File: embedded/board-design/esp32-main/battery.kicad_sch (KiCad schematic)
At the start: 1 part, among them U4 LTC4055

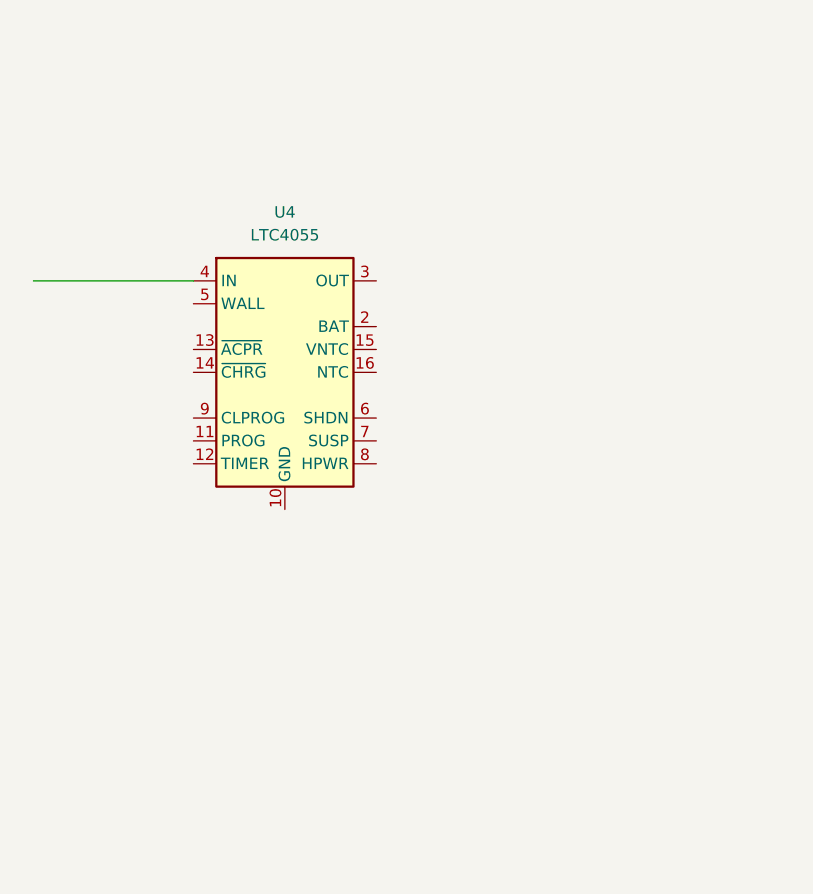
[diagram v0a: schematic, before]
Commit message: [bike-embedded-app]
Finished first schematic draft.

Signed-off-by: Nicolae-Andrei Vasile <vasilenicolaeandrei@gmail.com>
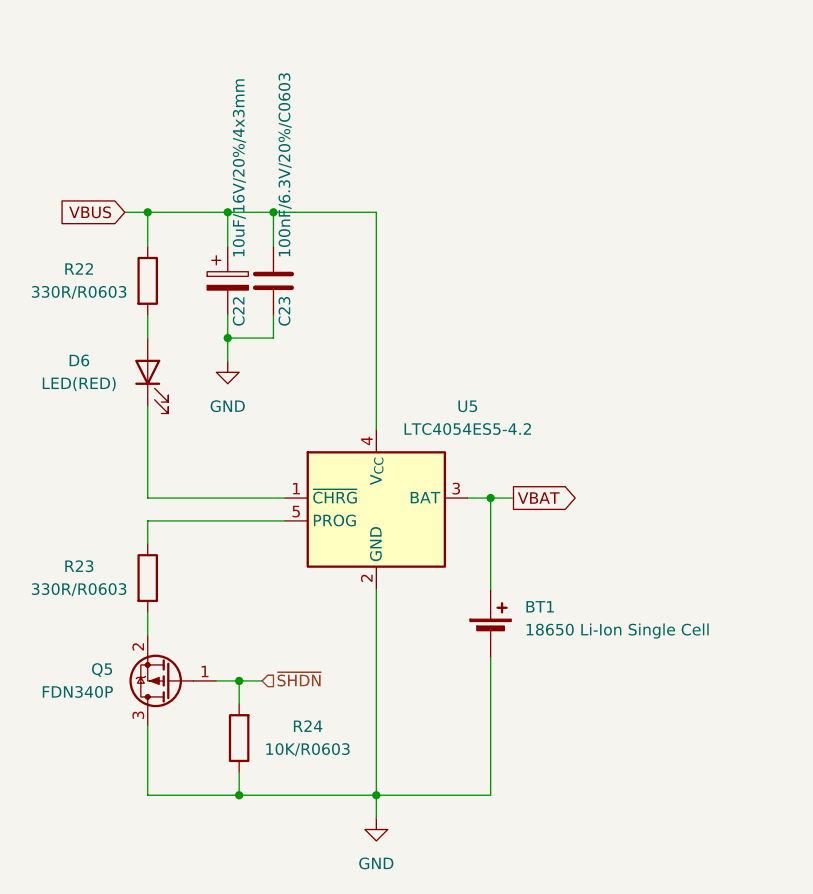
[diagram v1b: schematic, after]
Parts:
- removed U4: LTC4055, Package_DFN_QFN:QFN-16-1EP_4x4mm_P0.65mm_EP2.15x2.15mm, symbol Battery_Management:LTC4055
- added BT1: 18650 Li-Ion Single Cell, Battery:BatteryHolder_Keystone_1042_1x18650, symbol Device:Battery_Cell
- added C22: 10uF/16V/20%/4x3mm, Capacitor_SMD:CP_Elec_4x3, symbol Device:C_Polarized
- added C23: 100nF/6.3V/20%/C0603, Capacitor_SMD:C_0603_1608Metric_Pad1.08x0.95mm_HandSolder, symbol Device:C
- added D6: LED(RED), LED_SMD:LED_0603_1608Metric_Pad1.05x0.95mm_HandSolder, symbol Device:LED
- added Q5: FDN340P, Package_TO_SOT_SMD:SOT-23, symbol Transistor_FET:FDN340P
- added R22, R23: 330R/R0603, Resistor_SMD:R_0603_1608Metric_Pad0.98x0.95mm_HandSolder, symbol Device:R
- added R24: 10K/R0603, Resistor_SMD:R_0603_1608Metric_Pad0.98x0.95mm_HandSolder, symbol Device:R
- added U5: LTC4054ES5-4.2, Package_TO_SOT_SMD:TSOT-23-5, symbol Battery_Management:LTC4054ES5-4.2
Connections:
- new net: D6.2 (A), R22.2
- new net: Q5.2 (S), R23.2
- new net: D6.1 (K), U5.1 (~{CHRG})
- new net: R23.1, U5.5 (PROG)
- new net GND: BT1.2 (-), C22.2, C23.2, Q5.3 (D), R24.1, U5.2 (GND)
- new net VBAT: BT1.1 (+), U5.3 (BAT)
- new net VBUS: C22.1, C23.1, R22.1, U5.4 (V_{CC})
- new net ~{SHDN}: Q5.1 (G), R24.2

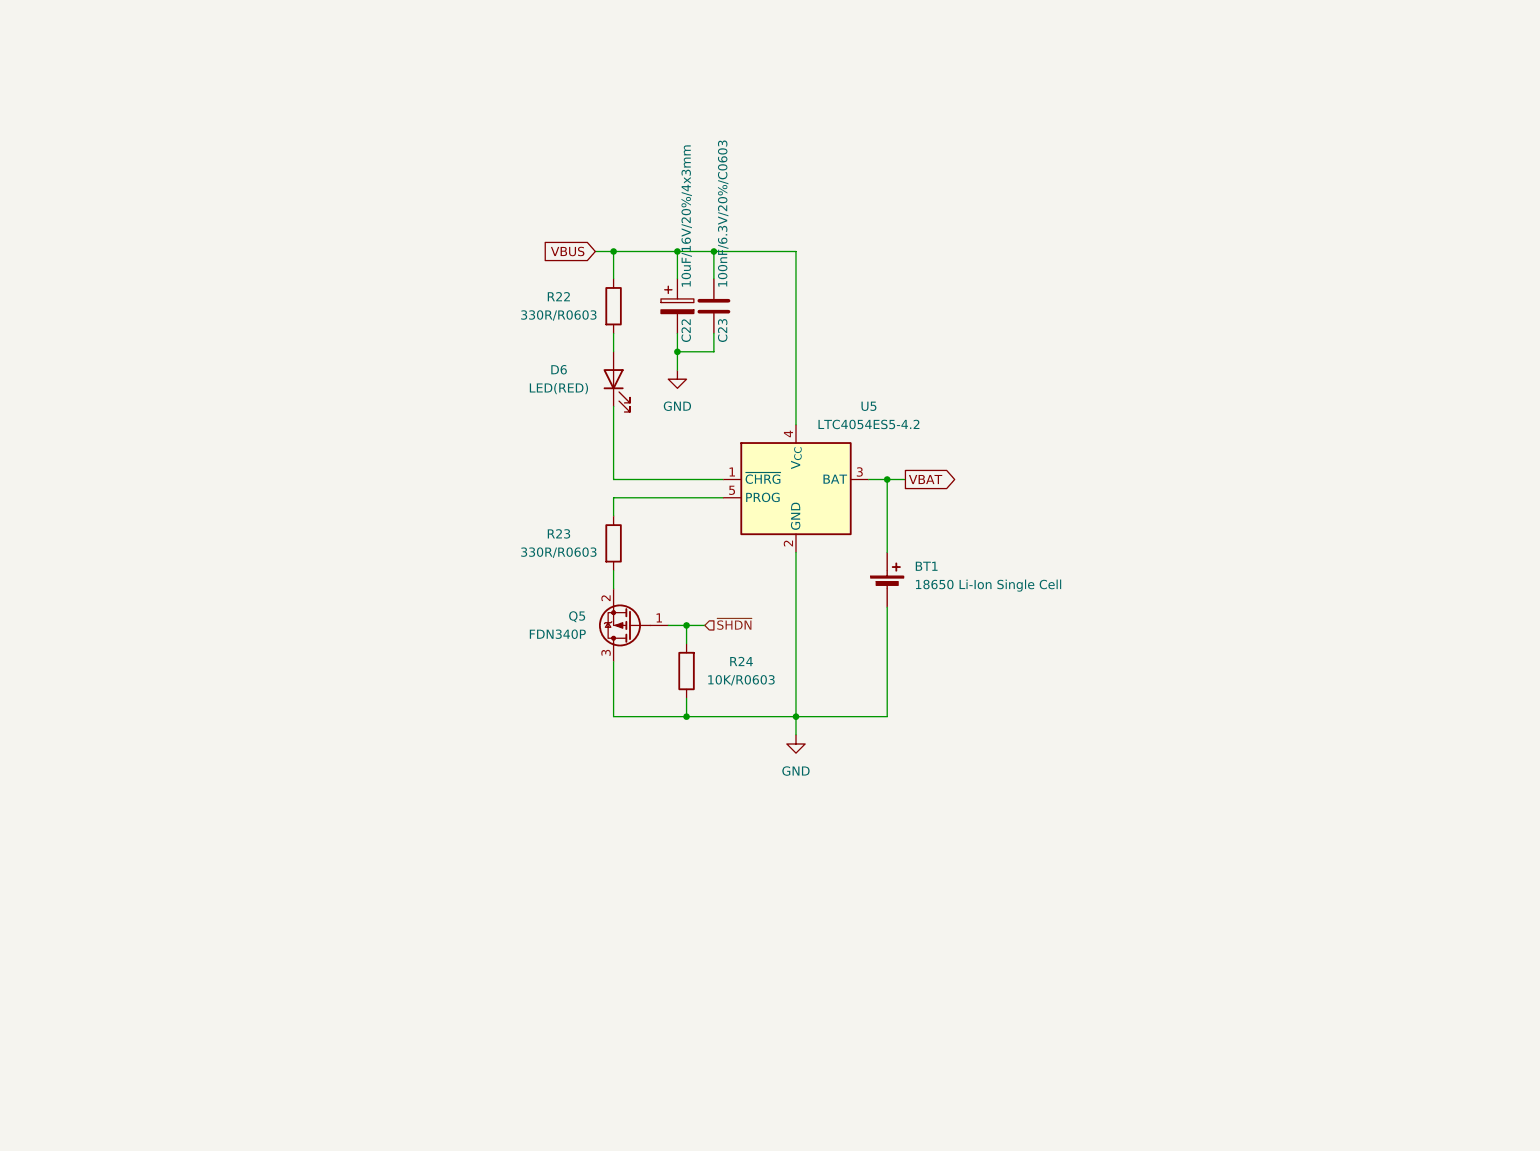
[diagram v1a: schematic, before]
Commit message: [bike-embedded-app]
First draft of the part placement on PCB. No routes drawn yet. Added
entry for possible alternator.

Signed-off-by: Nicolae-Andrei Vasile <vasilenicolaeandrei@gmail.com>
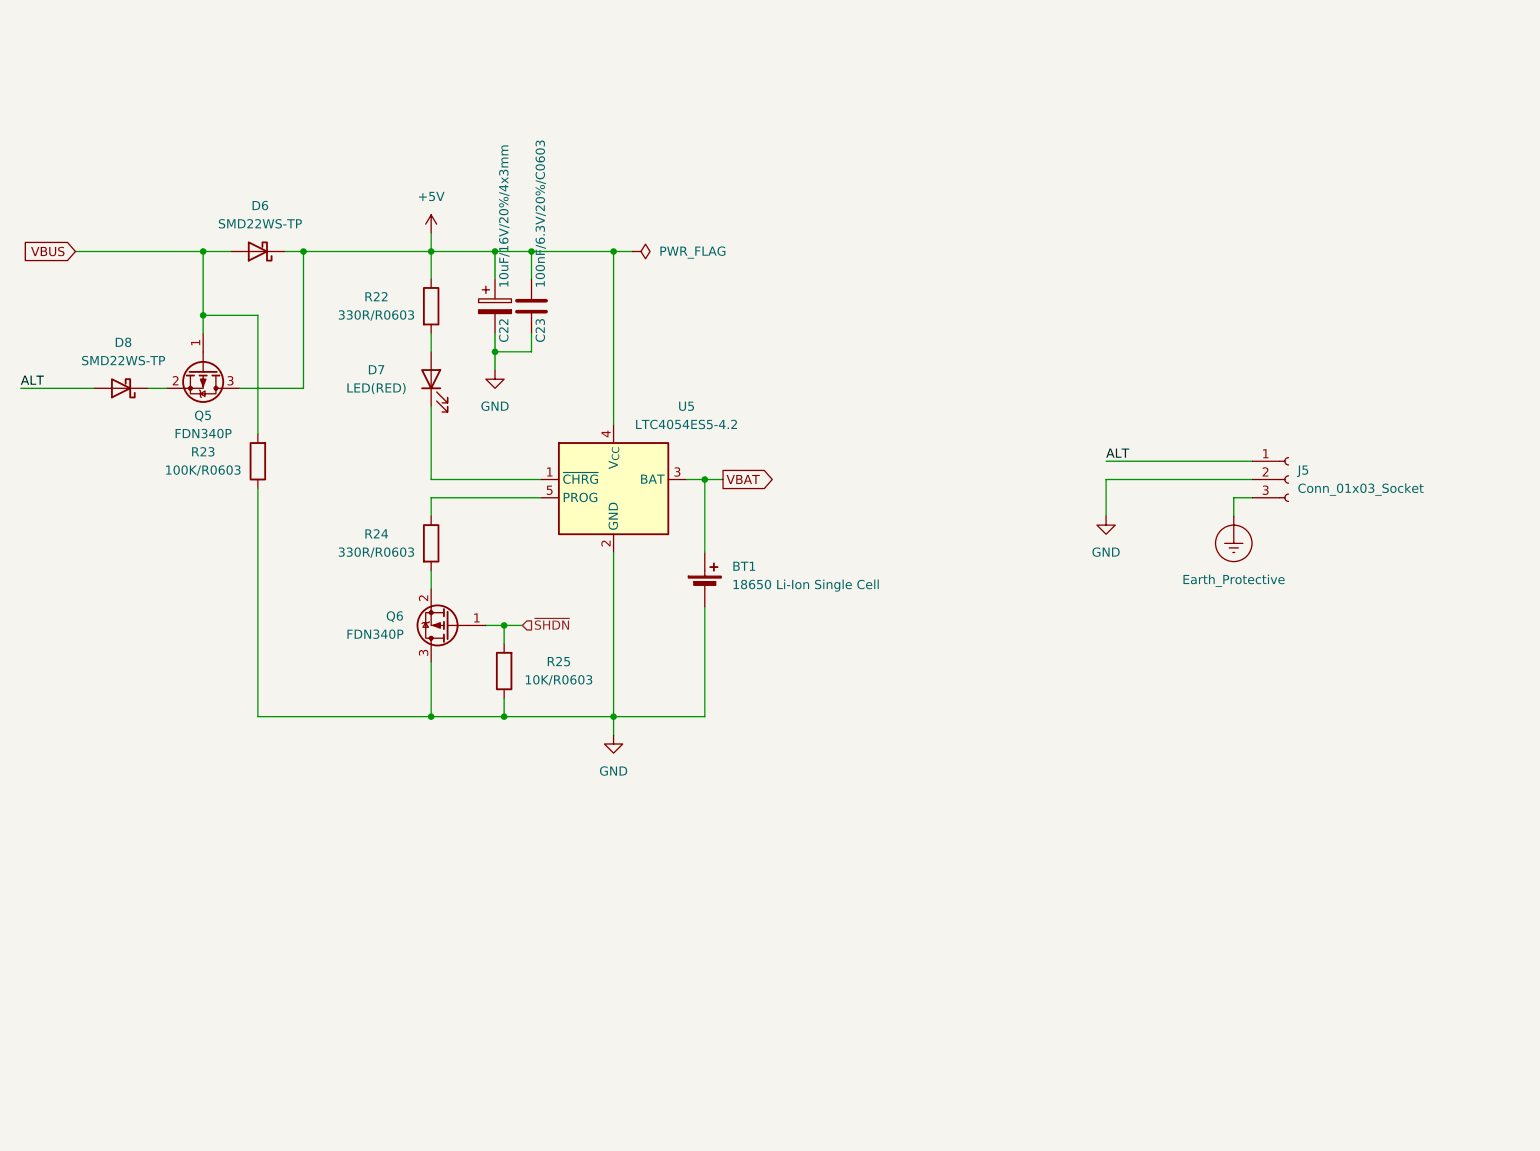
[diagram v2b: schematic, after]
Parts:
- added D6, D8: SMD22WS-TP, Diode_SMD:D_SOD-323_HandSoldering, symbol Device:D_Schottky
- added J5: Conn_01x03_Socket, Connector_Phoenix_MC:PhoenixContact_MC_1,5_3-G-3.81_1x03_P3.81mm_Horizontal, symbol Connector:Conn_01x03_Socket
- added Q5: FDN340P, Package_TO_SOT_SMD:SOT-23, symbol Transistor_FET:FDN340P
- added R23: 100K/R0603, Resistor_SMD:R_0603_1608Metric_Pad0.98x0.95mm_HandSolder, symbol Device:R
- renumbered D6 to D7, Q5 to Q6, R23 to R24, R24 to R25
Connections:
- net GND: now also J5.2 (Pin_2), R23.1
- net VBUS: now also D6.2 (A), Q5.1 (G), R23.2; no longer C22.1, C23.1, R22.1, U5.4 (V_{CC})
- new net: D8.1 (K), Q5.2 (S)
- new net +5V: C22.1, C23.1, D6.1 (K), Q5.3 (D), R22.1, U5.4 (V_{CC})
- new net ALT: D8.2 (A), J5.1 (Pin_1)
- new net Earth_Protective: J5.3 (Pin_3)
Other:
- moved on the sheet: BT1, C22, C23, D7, Q6, R22, R24, R25, U5

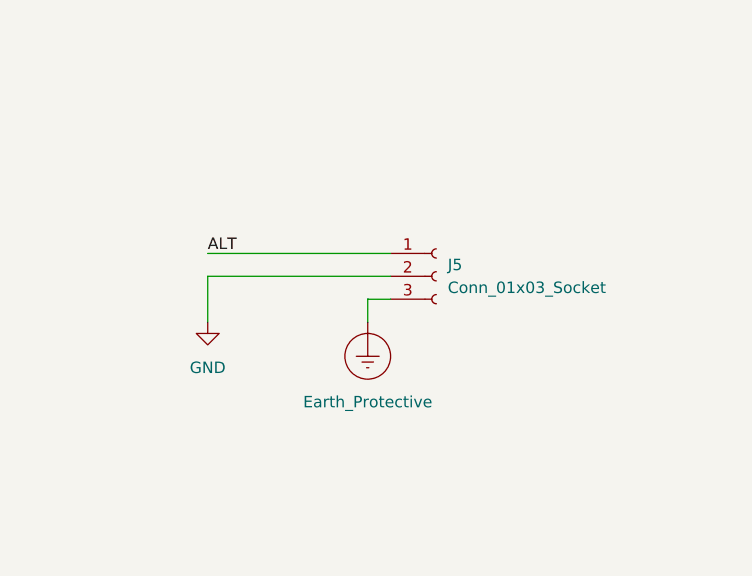
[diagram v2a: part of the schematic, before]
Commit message: [bike-embedded-app]
Finished first draft of the embedded hardware app. PCB design
constraints follow PCBWay recommendations.

Signed-off-by: Nicolae-Andrei Vasile <vasilenicolaeandrei@gmail.com>
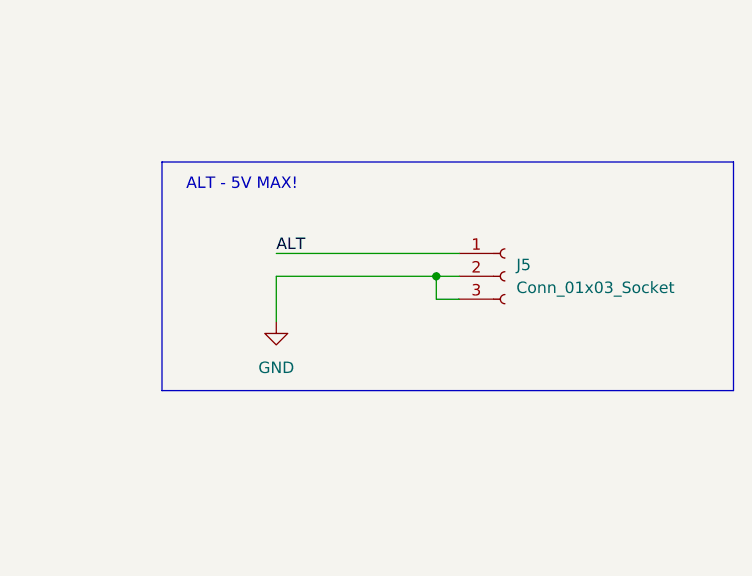
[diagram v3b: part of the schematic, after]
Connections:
- net Earth_Protective is gone; now on net GND: J5.3 (Pin_3)
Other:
- note added: "ALT - 5V MAX!"
- title: (none) -> ESP32 embedded application
- moved on the sheet: J5

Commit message: [bike-embedded-app]
Signed-off-by: Nicolae-Andrei Vasile <vasilenicolaeandrei@gmail.com>
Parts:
- renumbered J5 to J7
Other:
- moved on the sheet: BT1, C22, C23, D6, D7, D8, J7, Q5, Q6, R22, R23, R24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

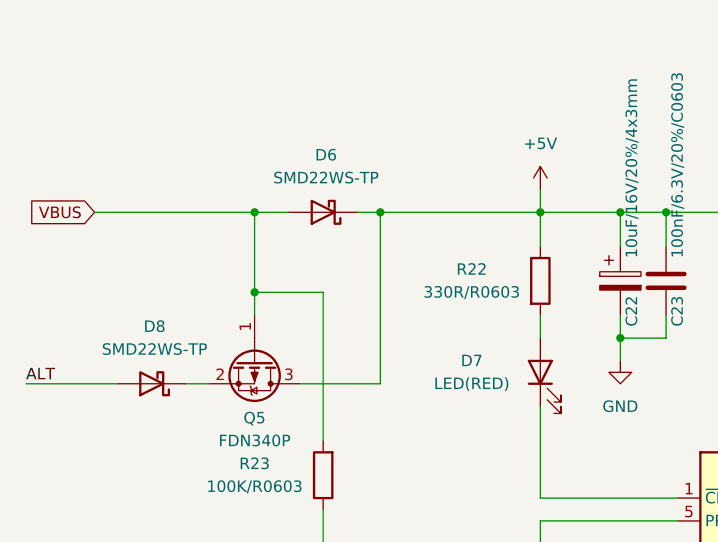
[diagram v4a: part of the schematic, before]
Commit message: [bike-embedded-app]
Added output for 3V3. Increased mounting holes.

Signed-off-by: Nicolae-Andrei Vasile <vasilenicolaeandrei@gmail.com>
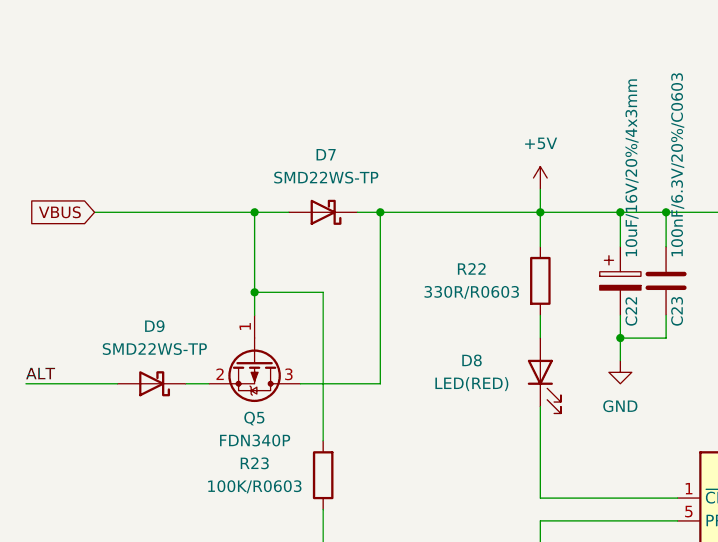
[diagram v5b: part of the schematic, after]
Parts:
- renumbered D6 to D7, D7 to D8, D8 to D9
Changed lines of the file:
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@@
 		(on_board yes)
 		(dnp no)
-		(property "Reference" "D6"
+		(property "Reference" "D7"
 			(at 109.5375 52.07 0)
 			(effects
@@
 			(project "esp32-main"
 				(path "/6d02e045-d1b3-4320-a4f8-f5e2c734acd4/9cfdfa29-fef4-49c3-96a5-094ec94d9453"
-					(reference "D6")
+					(reference "D7")
 					(unit 1)
 				)
@@
 		(dnp no)
 		(fields_autoplaced yes)
-		(property "Reference" "#PWR022"
+		(property "Reference" "#PWR024"
 			(at 133.35 59.69 0)
 			(effects
@@
 			(project ""
 				(path "/6d02e045-d1b3-4320-a4f8-f5e2c734acd4/9cfdfa29-fef4-49c3-96a5-094ec94d9453"
-					(reference "#PWR022")
+					(reference "#PWR024")
 					(unit 1)
 				)
@@
 		(dnp no)
 		(fields_autoplaced yes)
-		(property "Reference" "#PWR024"
+		(property "Reference" "#PWR026"
 			(at 158.75 132.08 0)
 			(effects
@@
 			(project "esp32-main"
 				(path "/6d02e045-d1b3-4320-a4f8-f5e2c734acd4/9cfdfa29-fef4-49c3-96a5-094ec94d9453"
-					(reference "#PWR024")
+					(reference "#PWR026")
 					(unit 1)
 				)
@@
 		(dnp no)
 		(fields_autoplaced yes)
-		(property "Reference" "#PWR025"
+		(property "Reference" "#PWR027"
 			(at 120.65 191.77 0)
 			(effects
@@
 			(project "esp32-main"
 				(path "/6d02e045-d1b3-4320-a4f8-f5e2c734acd4/9cfdfa29-fef4-49c3-96a5-094ec94d9453"
-					(reference "#PWR025")
+					(reference "#PWR027")
 					(unit 1)
 				)
@@
 		(on_board yes)
 		(dnp no)
-		(property "Reference" "D8"
+		(property "Reference" "D9"
 			(at 90.4875 71.12 0)
 			(effects
@@
 			(project "esp32-main"
 				(path "/6d02e045-d1b3-4320-a4f8-f5e2c734acd4/9cfdfa29-fef4-49c3-96a5-094ec94d9453"
-					(reference "D8")
+					(reference "D9")
 					(unit 1)
 				)
@@
 		(dnp no)
 		(fields_autoplaced yes)
-		(property "Reference" "#PWR023"
+		(property "Reference" "#PWR025"
 			(at 142.24 81.28 0)
 			(effects
@@
 			(project "esp32-main"
 				(path "/6d02e045-d1b3-4320-a4f8-f5e2c734acd4/9cfdfa29-fef4-49c3-96a5-094ec94d9453"
-					(reference "#PWR023")
+					(reference "#PWR025")
 					(unit 1)
 				)
@@
 		(on_board yes)
 		(dnp no)
-		(property "Reference" "D7"
+		(property "Reference" "D8"
 			(at 125.73 74.93 90)
 			(effects
@@
 			(project "esp32-main"
 				(path "/6d02e045-d1b3-4320-a4f8-f5e2c734acd4/9cfdfa29-fef4-49c3-96a5-094ec94d9453"
-					(reference "D7")
+					(reference "D8")
 					(unit 1)
 				)
